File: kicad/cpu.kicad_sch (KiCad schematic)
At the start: 20 parts, among them IC1 Z180, U16 74HC00, U20 74HC688, U21 74HC688, U23 74HC74, U27 74HC32, U8 74HC138, Y2 12.288 MHz

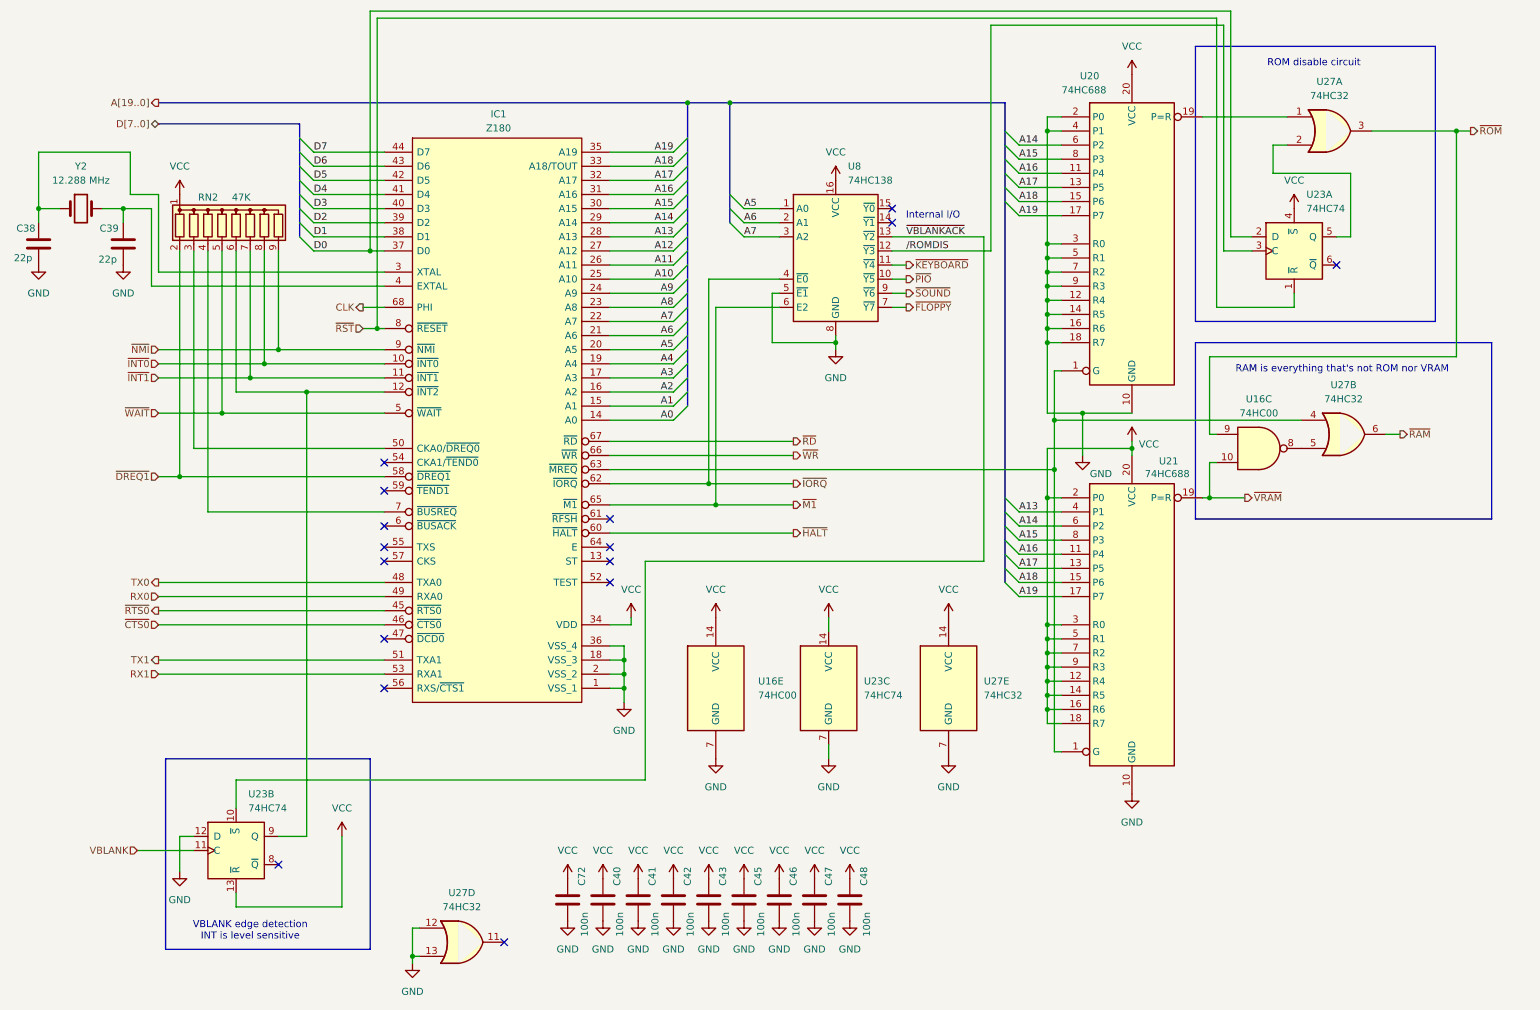
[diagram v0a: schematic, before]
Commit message: hw: simplify logic, replace some SSI with GALs
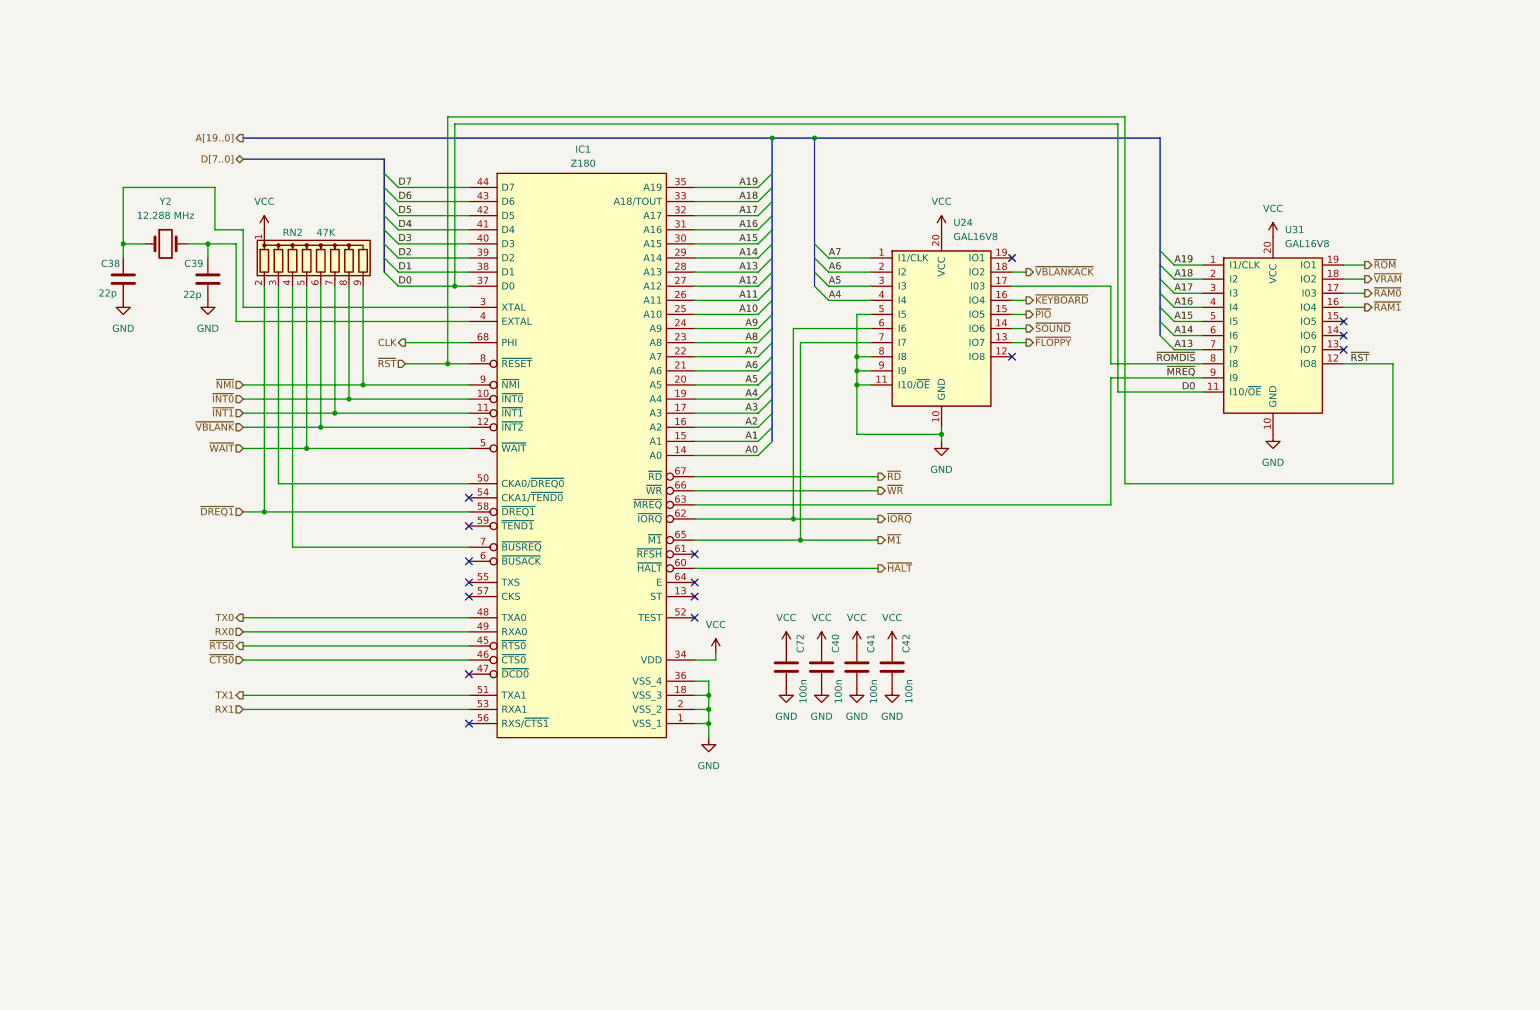
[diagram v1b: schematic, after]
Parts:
- removed C43, C45, C46, C47, C48: 100n, Capacitor_THT:C_Disc_D5.0mm_W2.5mm_P2.50mm, symbol Device:C
- removed U16: 74HC00, Package_DIP:DIP-14_W7.62mm, symbol 74xx:74HC00
- removed U20, U21: 74HC688, Package_DIP:DIP-20_W7.62mm, symbol 74xx:74HC688
- removed U23: 74HC74, Package_DIP:DIP-14_W7.62mm, symbol 74xx:74HC74
- removed U27: 74HC32, Package_DIP:DIP-14_W7.62mm, symbol 74xx:74LS32
- removed U8: 74HC138, Package_DIP:DIP-16_W7.62mm, symbol 74xx:74HC138
- added U24, U31: GAL16V8, Package_DIP:DIP-20_W7.62mm, symbol Logic_Programmable:GAL16V8
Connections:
- net A13: now also U31.7 (I7)
- net A14: now also U31.6 (I6)
- net A15: now also U31.5 (I5)
- net A16: now also U31.4 (I4)
- net A17: now also U31.3 (I3)
- net A18: now also U31.2 (I2)
- net A19: now also U31.1 (I1/CLK)
- net A4: now also U24.4 (I4)
- net A5: now also U24.3 (I3)
- net A6: now also U24.2 (I2)
- net A7: now also U24.1 (I1/CLK)
- net D0: now also U31.11 (I10/~{OE})
- net GND: now also U24.10 (GND), U24.11 (I10/~{OE}), U24.5 (I5), U24.8 (I8), U24.9 (I9), U31.10 (GND)
- net VCC: now also U24.20 (VCC), U31.20 (VCC)
- net ~{FLOPPY}: now also U24.13 (IO7)
- net ~{IORQ}: now also U24.6 (I6)
- net ~{KEYBOARD}: now also U24.16 (IO4)
- net ~{M1}: now also U24.7 (I7)
- net ~{PIO}: now also U24.15 (IO5)
- net ~{ROM}: now also U31.19 (IO1)
- net ~{RST}: now also U31.12 (IO8)
- net ~{SOUND}: now also U24.14 (IO6)
- net ~{VBLANKACK}: now also U24.18 (IO2)
- net ~{VRAM}: now also U31.18 (IO2)
- net ~{MREQ}: now reaches IC1.63 (~{MREQ})
- net ~{MREQ}: now also U31.9 (I9)
- net ~{VBLANK}: now reaches IC1.12 (~{INT2}), RN2.6 (R5)
- new net ~{RAM0}: U31.17 (I03)
- new net ~{RAM1}: U31.16 (IO4)
- new net ~{ROMDIS}: U24.17 (I03), U31.8 (I8)
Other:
- note removed: "Internal I/O"
- note removed: "RAM is everything that's not ROM nor VRAM"
- note removed: "ROM disable circuit"
- note removed: "VBLANK edge detection INT is level sensitive"
- moved on the sheet: C38, C39, C40, C41, C42, C72, IC1, RN2, Y2
